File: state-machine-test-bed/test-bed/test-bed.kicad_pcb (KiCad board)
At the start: 2 copper layers, 18 parts

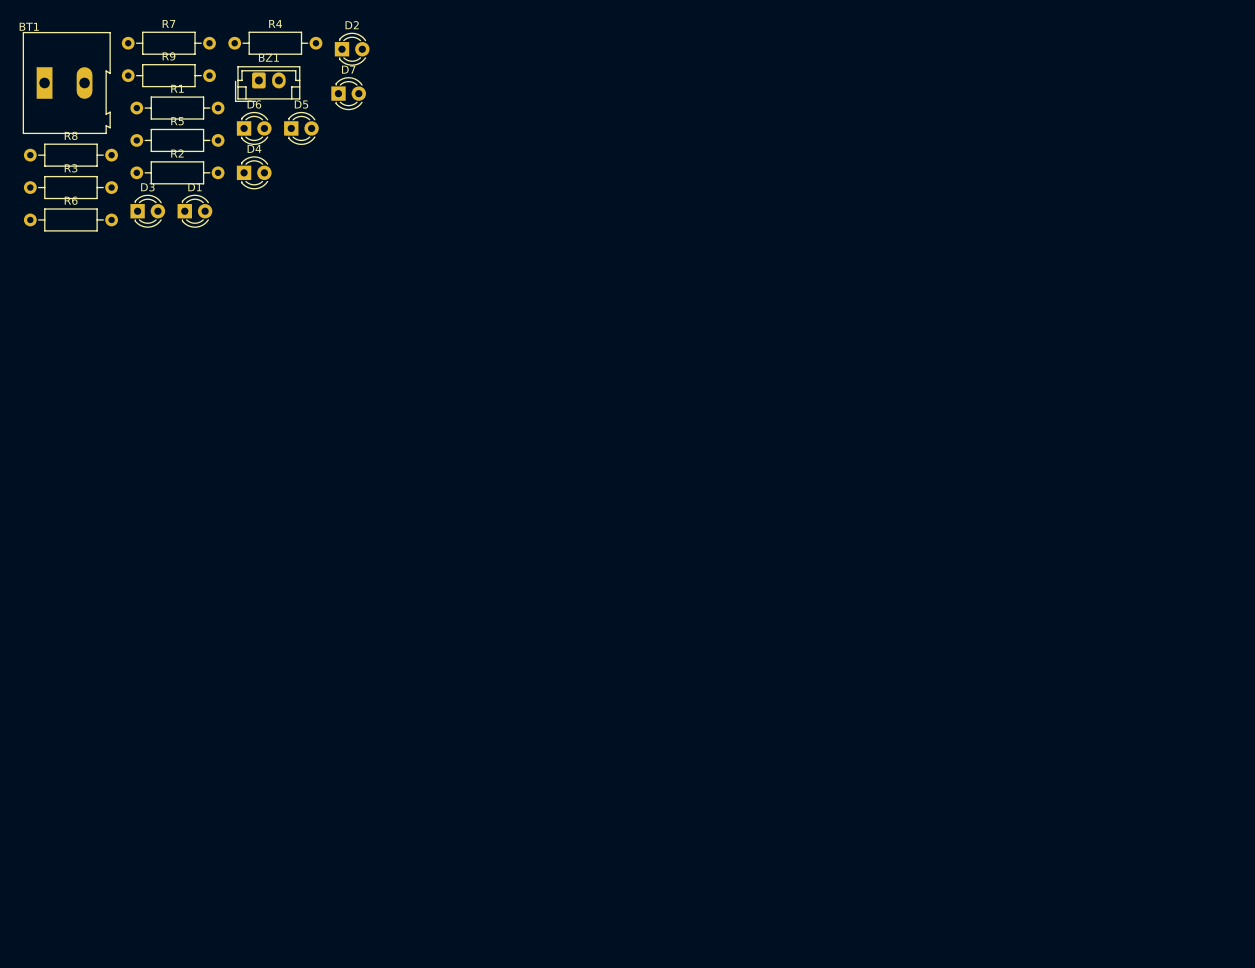
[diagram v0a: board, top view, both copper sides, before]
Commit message: finished routing for state-machine test board
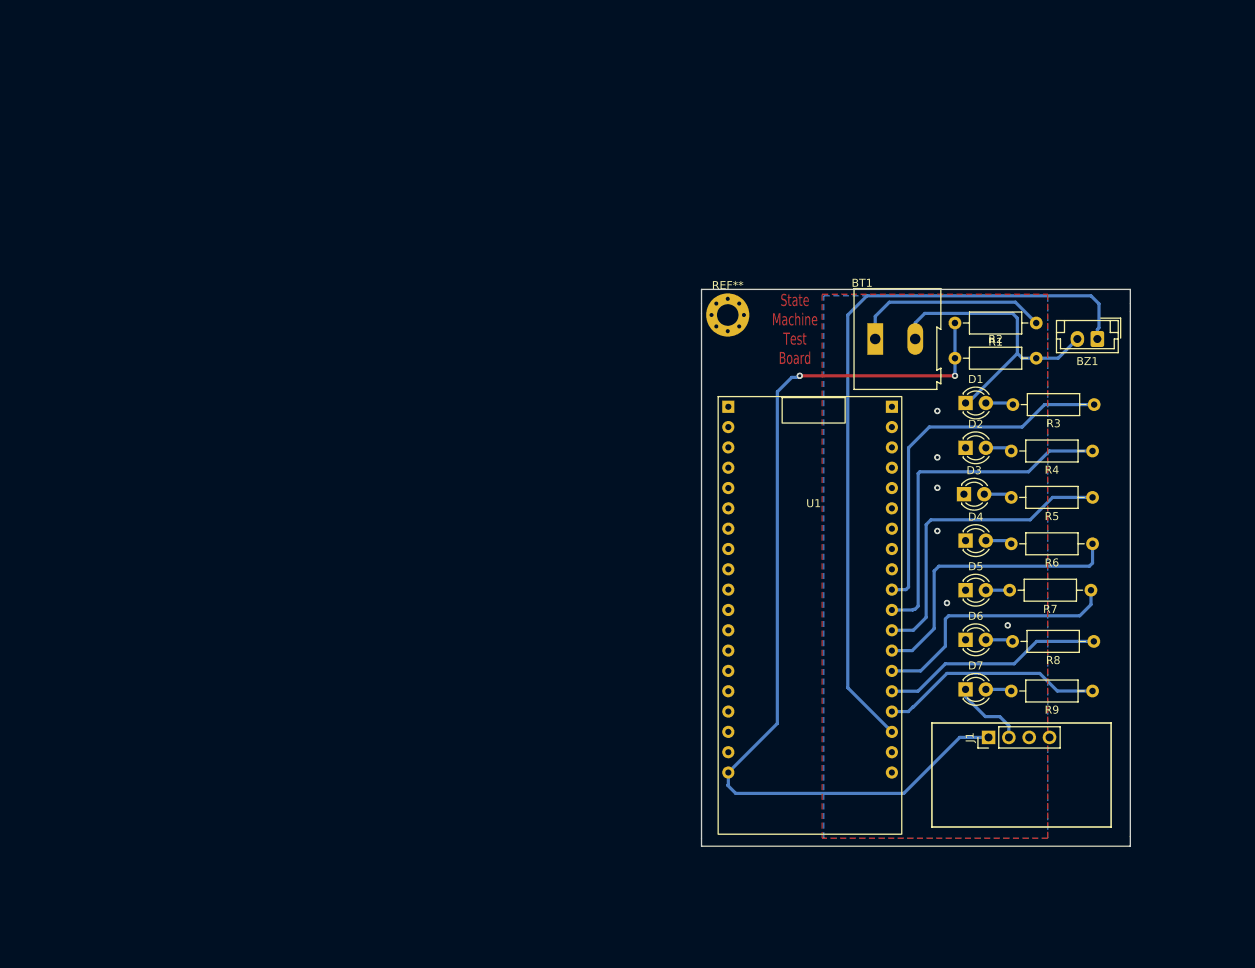
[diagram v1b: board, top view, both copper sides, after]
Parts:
- added J1: SSD1306, Connector_PinHeader_2.54mm:PinHeader_1x04_P2.54mm_Vertical, F.Cu at (159.6, 120.0)
- added REF**: MountingHole_2.7mm_M2.5_Pad_Via, MountingHole:MountingHole_2.7mm_M2.5_Pad_Via, F.Cu at (127.0, 67.2)
- added U1: NodeMCU, custom-footprints:NODEMCU, F.Cu at (125.8, 77.4)
- moved R8 146.2 mm to (172.8, 108.0), turned to 180 degrees
- moved R9 143.0 mm to (172.6, 114.2), turned to 180 degrees
- moved R6 138.8 mm to (172.6, 95.8), turned to 180 degrees
- moved R7 138.4 mm to (172.4, 101.6), turned to 180 degrees
- moved R3 135.7 mm to (172.8, 78.4), turned to 180 degrees
- moved R5 127.5 mm to (172.6, 90.0), turned to 180 degrees
- moved R4 118.7 mm to (172.6, 84.2), turned to 180 degrees
- moved R1 115.6 mm to (165.6, 68.2), turned to 180 degrees
- moved D6 110.5 mm to (156.7, 107.8)
- moved BZ1 109.7 mm to (173.2, 70.2), turned to 180 degrees
- moved D3 109.2 mm to (156.5, 89.6)
- moved BT1 108.7 mm to (145.4, 70.2)
- moved D7 108.1 mm to (156.7, 114.0)
- moved R2 104.9 mm to (155.4, 72.6)
- moved D5 102.2 mm to (156.7, 101.6)
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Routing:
- net 5V: track 0.00 -> 117.3 mm, vias 0 -> 2
- net BUZZER: track 0.00 -> 91.7 mm
- net GND: track 0.00 -> 47.0 mm, vias 0 -> 5
- net POST-FLIGHT: track 0.00 -> 45.1 mm
- net CHUTE-DESCENT: track 0.00 -> 43.0 mm
- net BALLISTIC-DESCENT: track 0.00 -> 38.8 mm
- net APOGEE: track 0.00 -> 36.2 mm
- net COASTING: track 0.00 -> 32.1 mm
- net PRE-FLIGHT: track 0.00 -> 28.0 mm
- net POWERED-FLIGHT: track 0.00 -> 27.8 mm
- net Net-(BT1-Pad1): track 0.00 -> 24.8 mm
- net Net-(D3-Pad2): track 0.00 -> 3.54 mm
- net Net-(D1-Pad2): track 0.00 -> 3.46 mm
- net Net-(D6-Pad2): track 0.00 -> 3.42 mm
- net Net-(D2-Pad2): track 0.00 -> 3.34 mm
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- added copper zone on B.Cu, net GND
- added copper zone on F.Cu, net GND
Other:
- board outline added: 53.6 x 69.6 mm
- board text added: "State Machine Test Board"

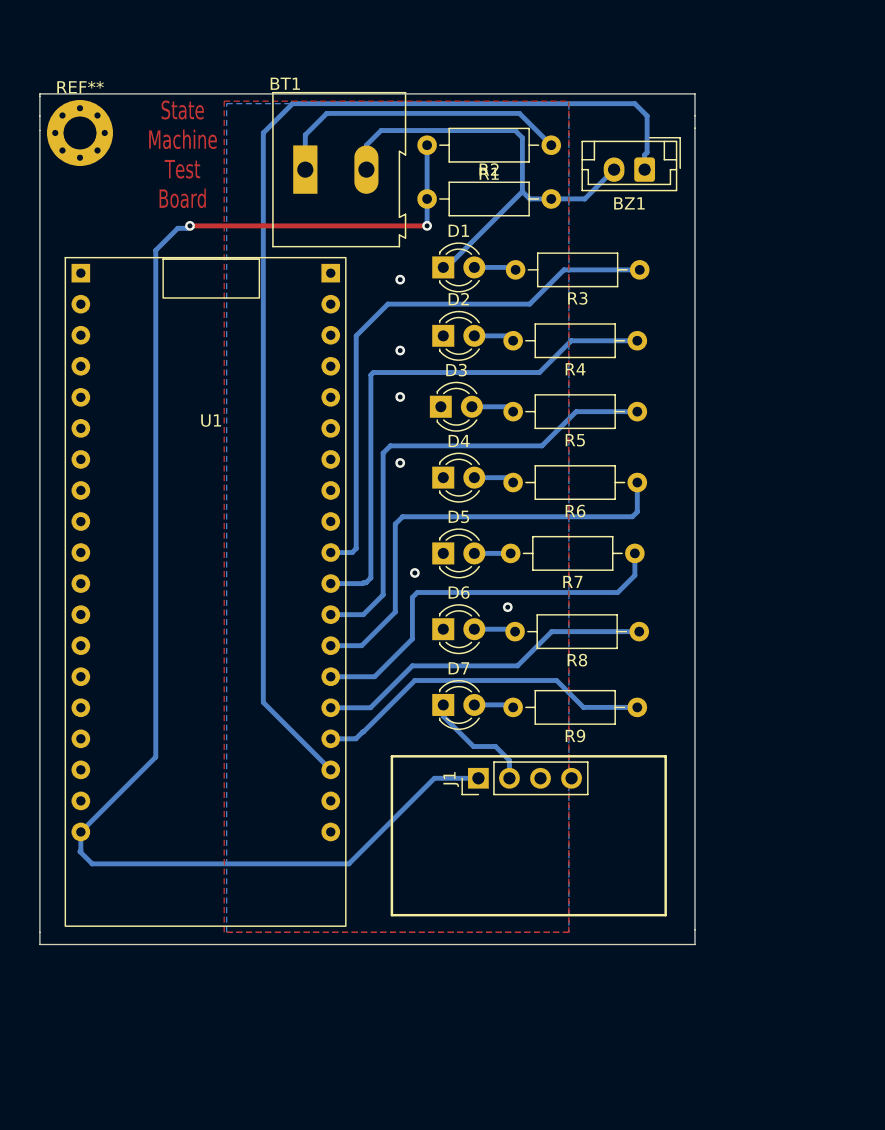
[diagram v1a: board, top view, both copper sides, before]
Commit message: finished routing for state-machine test board
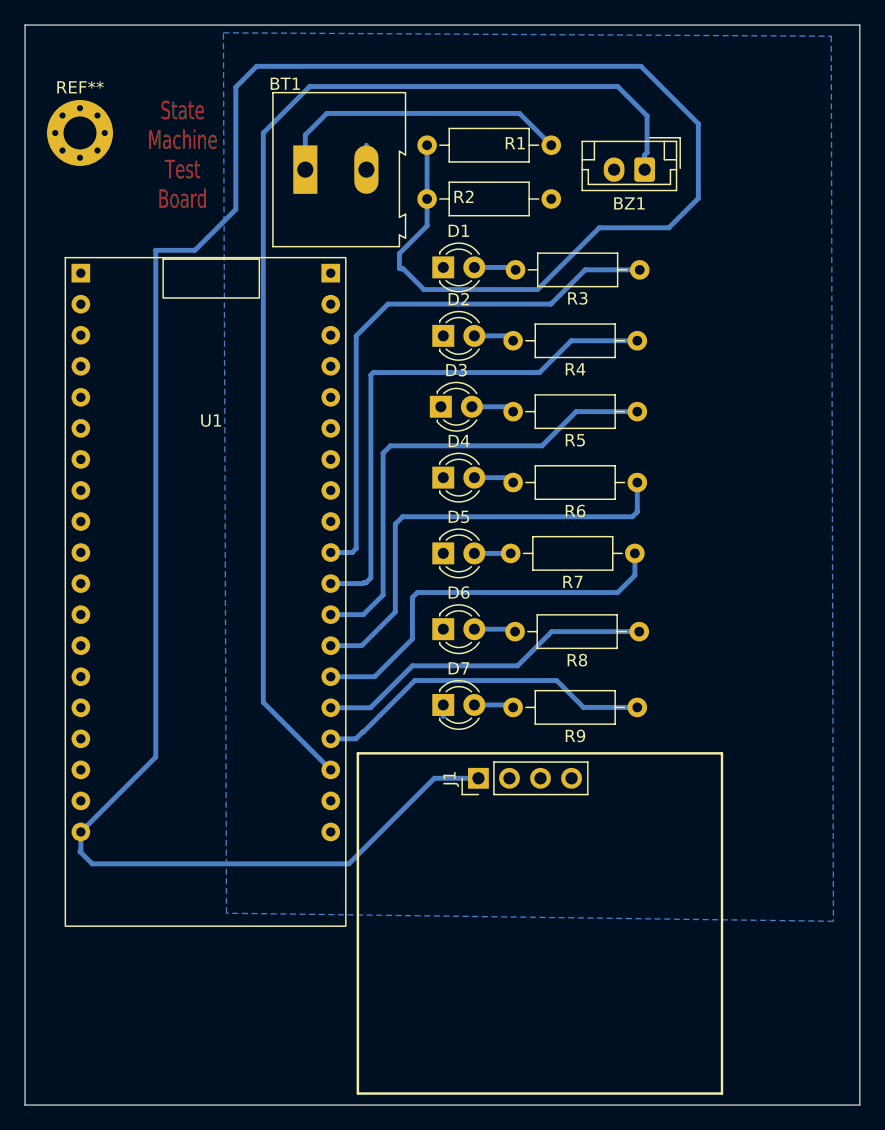
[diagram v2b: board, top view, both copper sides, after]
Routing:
- net 5V: track 117.3 -> 191.5 mm, vias 2 -> 0
- net GND: track 47.0 -> 3.20 mm, vias 5 -> 0
- net BUZZER: track 91.7 -> 92.8 mm
- net (no net): vias 1 -> 0
- removed copper zone on F.Cu, net GND
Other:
- board size 53.6 x 69.6 mm -> 68.3 x 88.4 mm
